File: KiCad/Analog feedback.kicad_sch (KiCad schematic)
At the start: 30 parts, among them U2 GS8332SR, U3 GS8332SR

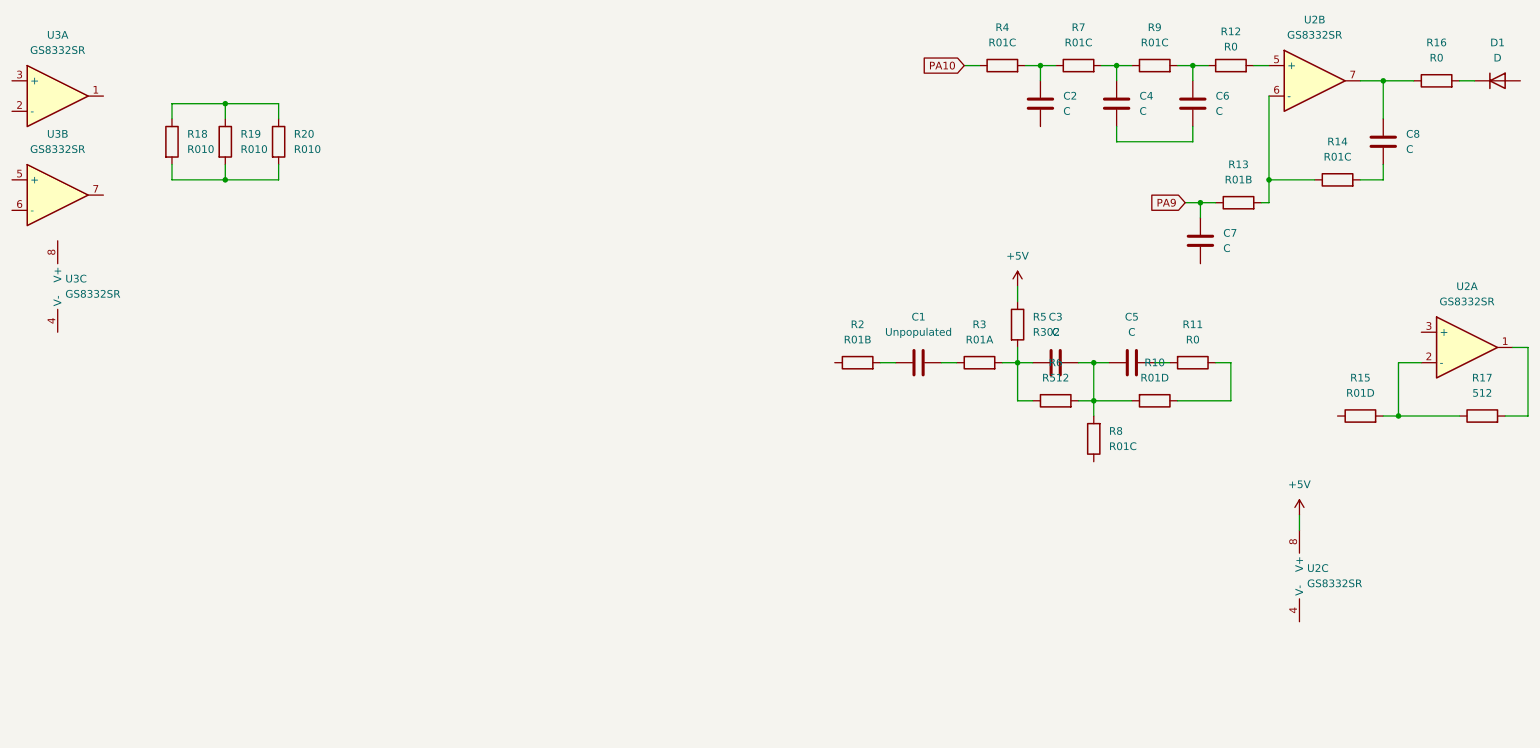
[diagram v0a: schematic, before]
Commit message: Added U4(LM321)
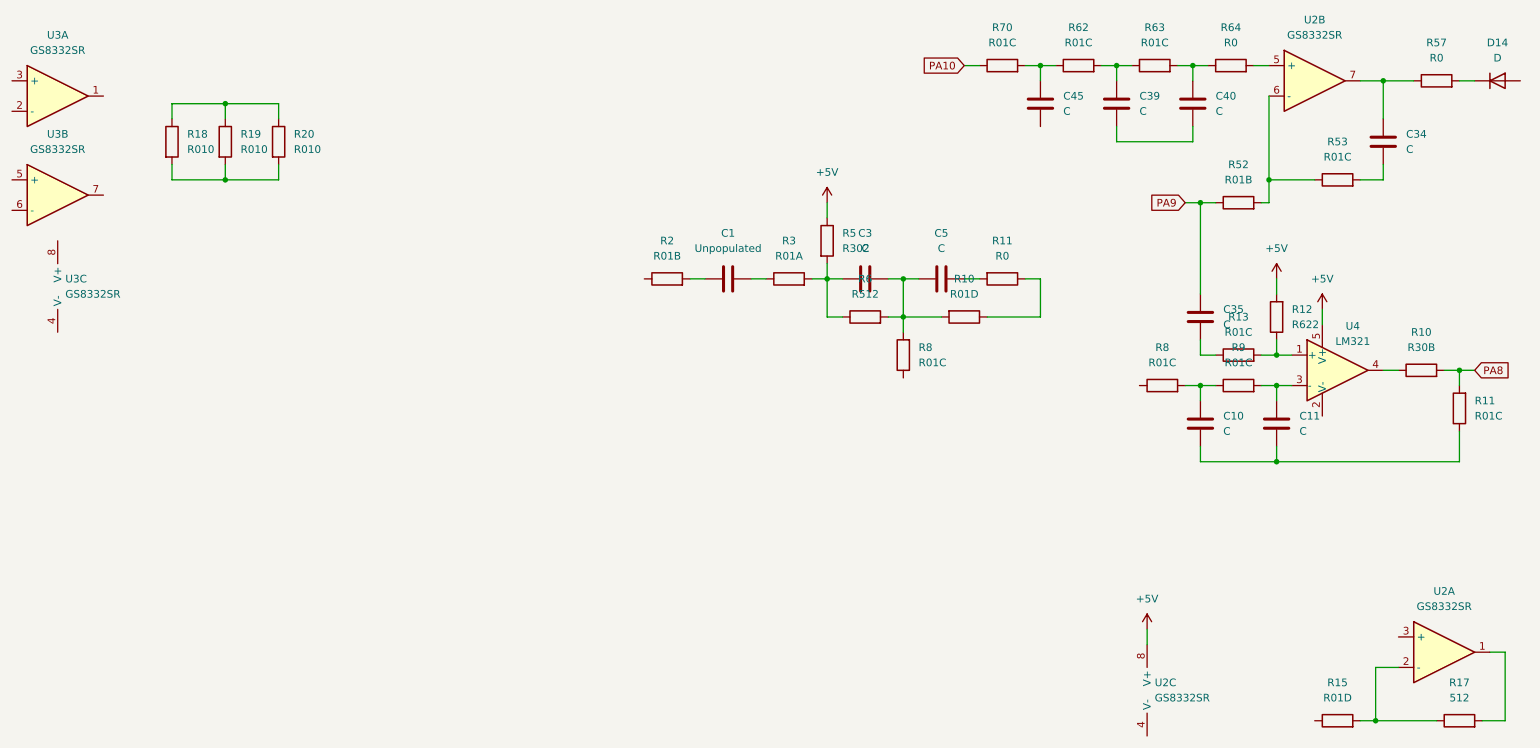
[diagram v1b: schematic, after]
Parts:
- added C10, C11: C, symbol Device:C
- added R10: R30B, symbol Device:R
- added R11, R13, R8, R9: R01C, symbol Device:R
- added R12: R622, symbol Device:R
- added U4: LM321, Package_TO_SOT_SMD:SOT-23-5, symbol Amplifier_Operational:LM321
- renumbered C8 to C34, C7 to C35, C4 to C39, C6 to C40, C2 to C45, D1 to D14, R13 to R52, R14 to R53, R16 to R57, R7 to R62, R9 to R63, R12 to R64, R4 to R70
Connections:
- net +5V: now also R12.2, U4.5 (V+)
- net at C35.2: now also R13.1
- new net: C10.2, R8.2, R9.1
- new net: R10.1, U4.4
- new net: C11.2, R9.2, U4.3 (-)
- new net: R12.1, R13.2, U4.1 (+)
- new net: C10.1, C11.1, R11.1
- new net PA8: R10.2, R11.2
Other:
- moved on the sheet: C1, C3, C35, C5, R10, R11, R15, R17, R2, R3, R5, R6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

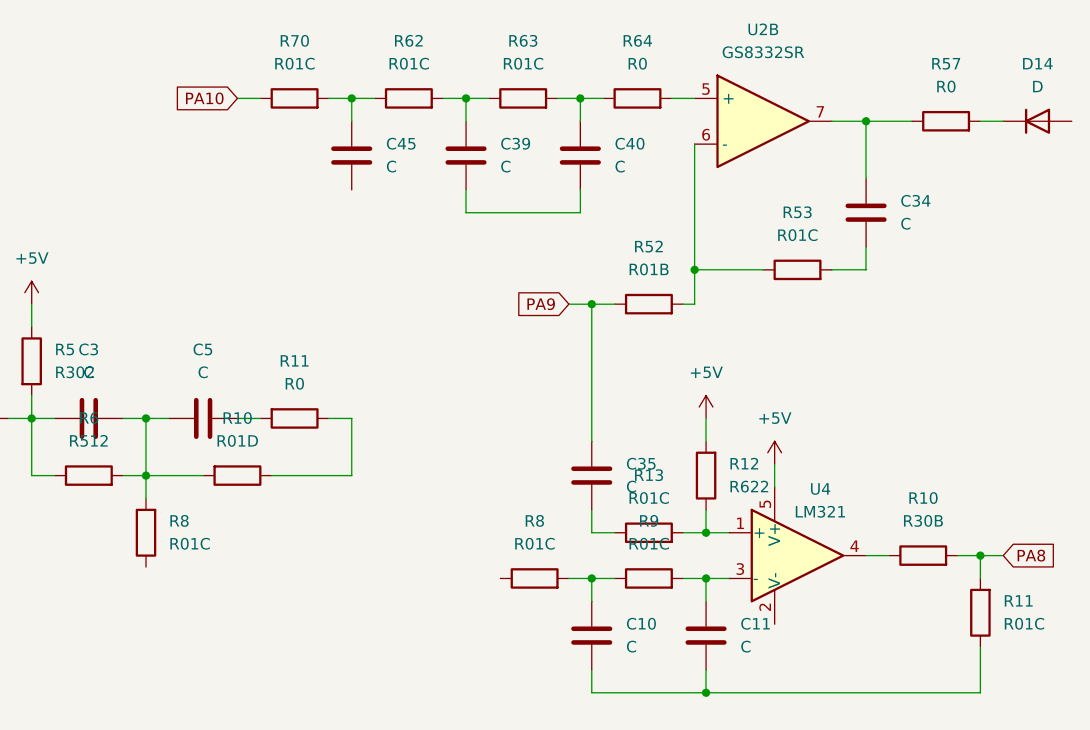
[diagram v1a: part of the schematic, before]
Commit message: Ooops AT32F421 pins were wrong. Didn't look at the pin designator. fixed now
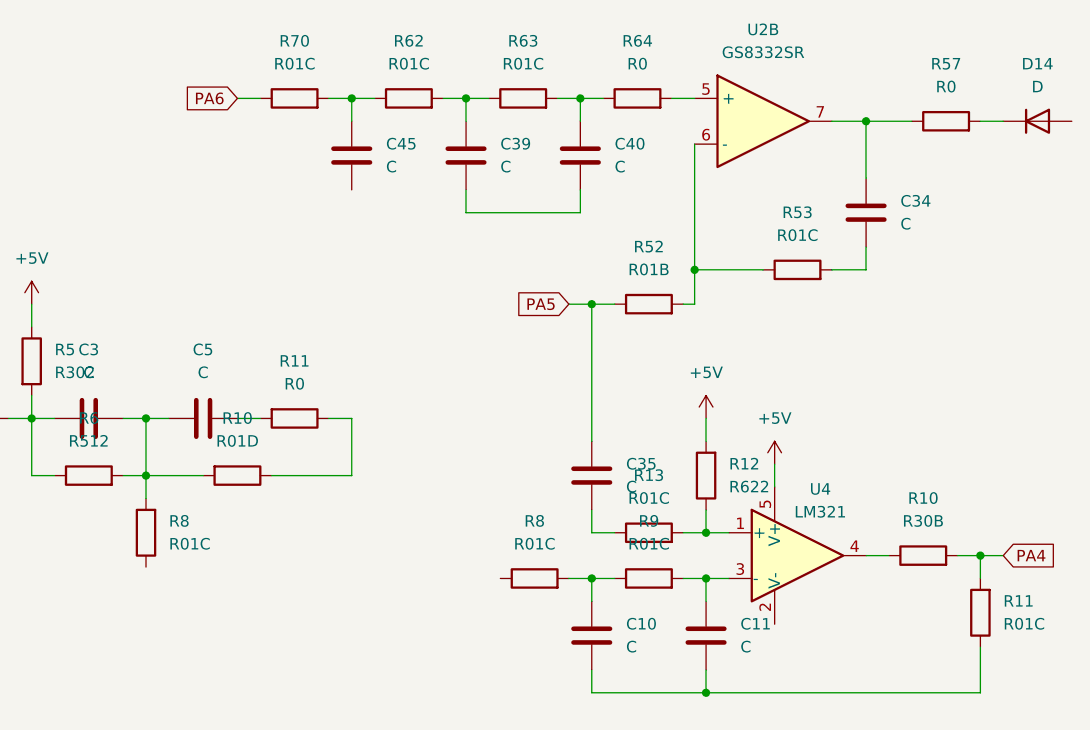
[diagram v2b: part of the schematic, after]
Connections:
- net PA10 renamed PA6
- net PA8 renamed PA4
- net PA9 renamed PA5
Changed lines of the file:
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@@
 		)
 	)
-	(global_label "PA8"
+	(global_label "PA4"
 		(shape input)
 		(at 266.7 76.2 0)
@@
 		)
 	)
-	(global_label "PA10"
+	(global_label "PA6"
 		(shape input)
 		(at 181.61 25.4 180)
@@
 		)
 		(property "Intersheetrefs" "${INTERSHEET_REFS}"
-			(at 173.8472 25.4 0)
+			(at 175.0567 25.4 0)
 			(effects
 				(font
@@
 		)
 	)
-	(global_label "PA9"
+	(global_label "PA5"
 		(shape input)
 		(at 218.44 48.26 180)
